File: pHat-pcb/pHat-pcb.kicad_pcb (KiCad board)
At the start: 2 copper layers, 65 x 30 mm, 21 parts, among them J1 Conn_02x20_Odd_Even, J2 Conn_01x24_Male, J3 Conn_Active_High, J4 Conn_Bat, J5 Conn_I2C, J8 Conn_Active_Low, SW1 SW_Push, U1 TPS61023_Breakout, U2 74HC74, U3 DS3231M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

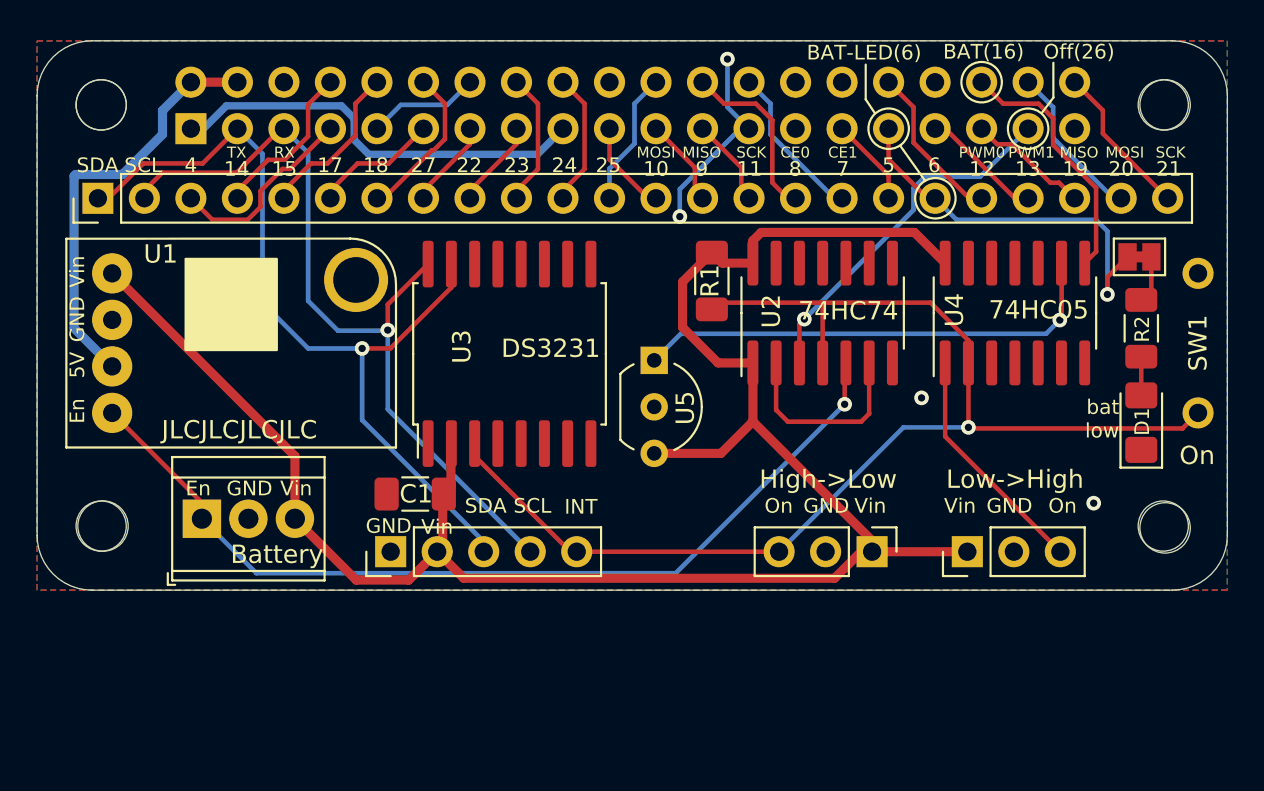
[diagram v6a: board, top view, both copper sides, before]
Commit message: Rev6: add connector for 5V, 3V3 and GND
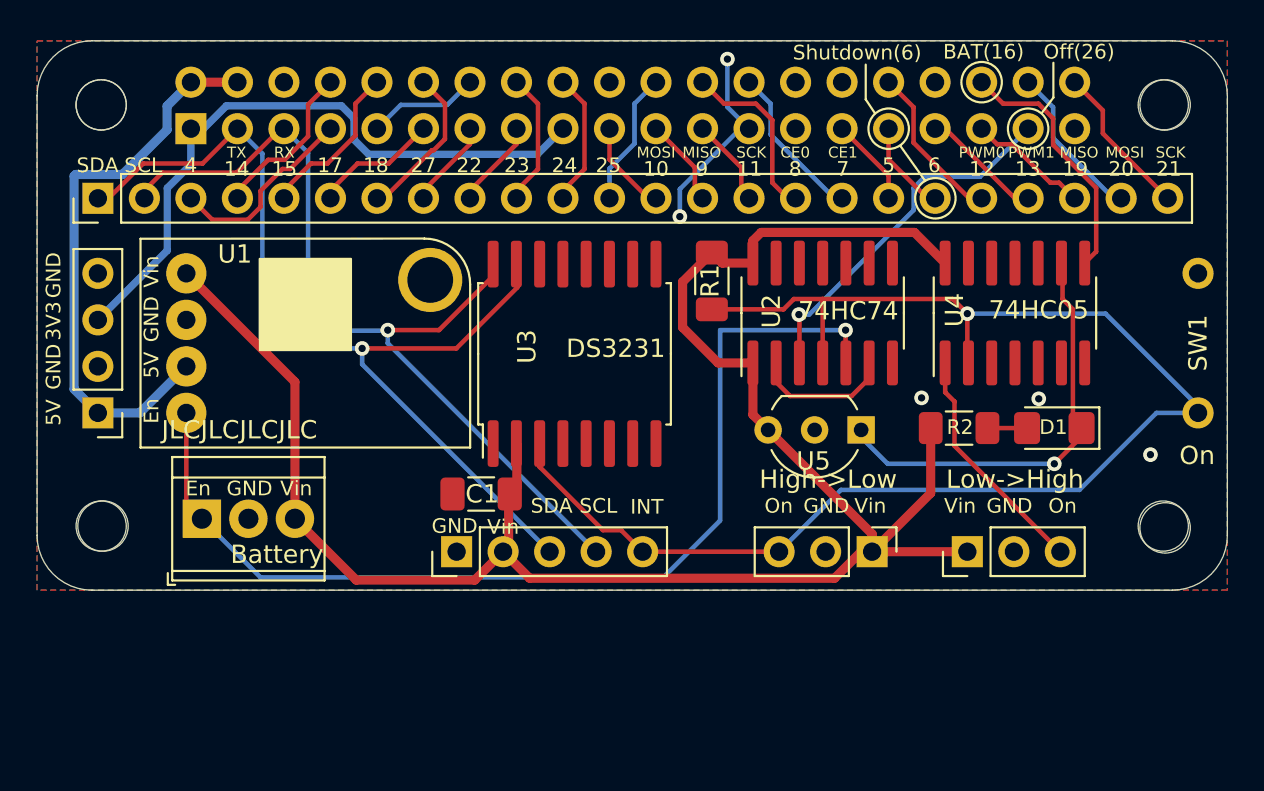
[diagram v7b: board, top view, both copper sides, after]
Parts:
- removed JP1: SolderJumper_2_Bridged, Jumper:SolderJumper-2_P1.3mm_Bridged_Pad1.0x1.5mm
- added J6: Conn_01x04_Male, Connector_PinHeader_2.54mm:PinHeader_1x04_P2.54mm_Vertical, F.Cu at (53.3, 69.3)
- moved U5 11.9 mm to (95.0, 70.2), turned to 180 degrees
- moved R2 11.3 mm to (100.3, 70.2), turned to 180 degrees
- moved D1 4.76 mm to (105.5, 70.2), turned to 180 degrees
- moved U1 4.05 mm to (58.1, 61.7)
- moved C1 3.60 mm to (74.2, 73.8)
- moved J5 3.60 mm to (72.9, 76.9)
- moved U3 3.55 mm to (79.3, 66.1)
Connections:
- D1 pad 1: GND -> /BatOk
- R2 pad 2: Net-(JP1-Pad1) -> /Vin
- U4 pad 9: /BatLow -> /BatOk
- U5 pad 1: /BatLow -> /BatOk
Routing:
- net /BatLow: track 26.2 -> 0.00 mm, vias 1 -> 0
- net /BatOk: track 0.00 -> 23.7 mm, vias 0 -> 1
- net /GPIO6: track 20.8 -> 4.68 mm, vias 1 -> 0
- net +3V3: track 23.2 -> 35.7 mm
- net /1~PRE: track 69.3 -> 79.8 mm
- net +5V: track 23.1 -> 31.2 mm
- net /En: track 50.3 -> 56.3 mm
- net /GPIO2(SDA1): track 46.8 -> 52.2 mm
- net /GPIO3(SCL1): track 44.4 -> 49.0 mm
- net Net-(U2-Pad2): track 10.9 -> 7.69 mm
- net Net-(JP1-Pad1): track 2.58 -> 0.00 mm
- net /Vin: track 107.1 -> 107.9 mm
- net Net-(J3-Pad3): track 13.5 -> 12.9 mm
- net GND: vias 4 -> 5
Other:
- board text added: "3V3"
- board text added: "5V"
- board text added: "Rev 6"
- board text added: "Shutdown(6)"
- board text removed: "BAT-LED(6)"
- board text removed: "Rev 5"
- board text removed: "bat low"

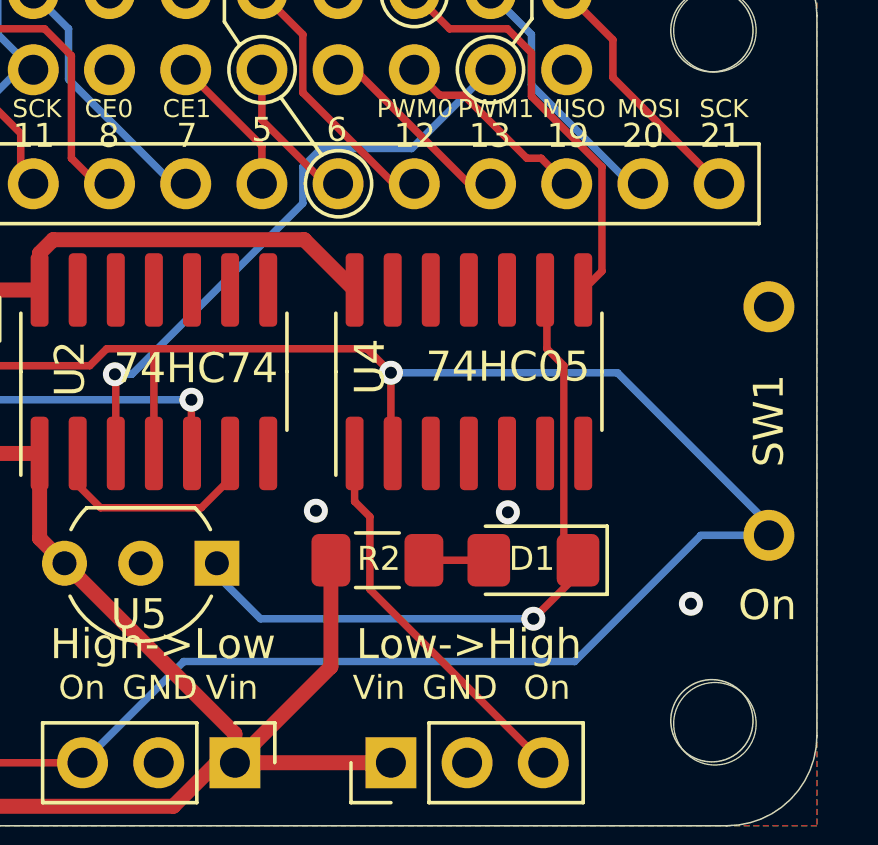
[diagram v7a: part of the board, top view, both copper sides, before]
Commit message: Rev7: added shutdown-button
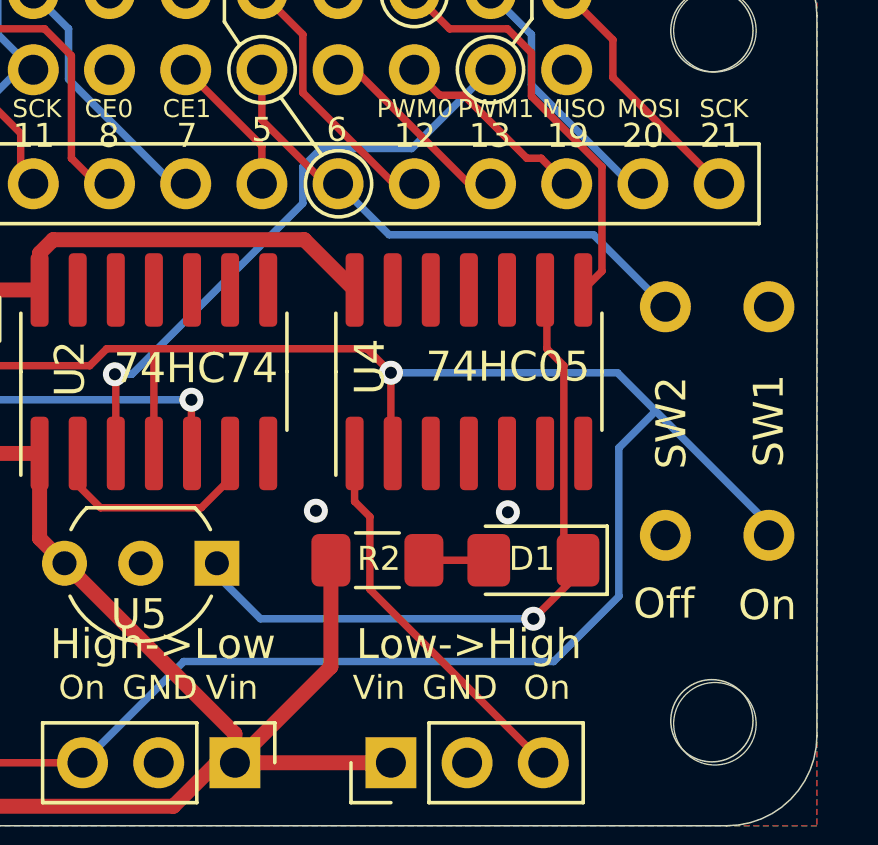
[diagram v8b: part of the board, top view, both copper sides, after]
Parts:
- added SW2: SW_Push, user:SW_PUSH_SLIM_1x4, F.Cu at (110.0, 69.3)
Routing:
- net /GPIO6: track 4.68 -> 17.3 mm
- net /1~PRE: track 79.8 -> 81.3 mm
- net GND: vias 5 -> 4
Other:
- board text added: "Off"
- board text added: "Rev 7"
- board text removed: "Rev 6"
